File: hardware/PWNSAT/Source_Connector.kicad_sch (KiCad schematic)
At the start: 4 parts

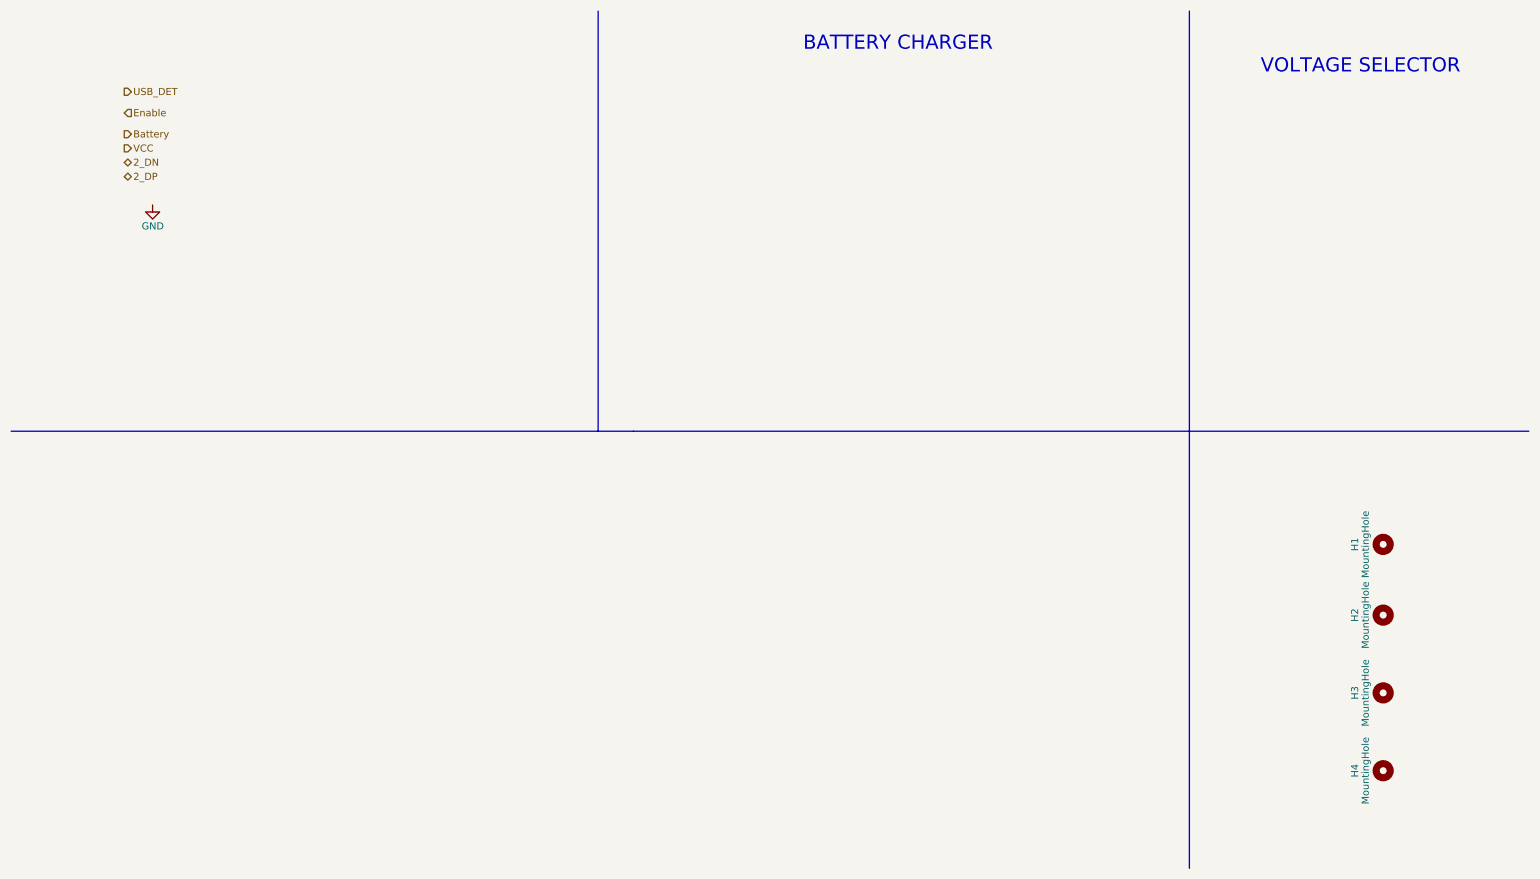
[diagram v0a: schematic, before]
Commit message: feat(Hw):Update_Battery_Sch_And_Sensors_And_PWNCube
pending_Outputs_connectors
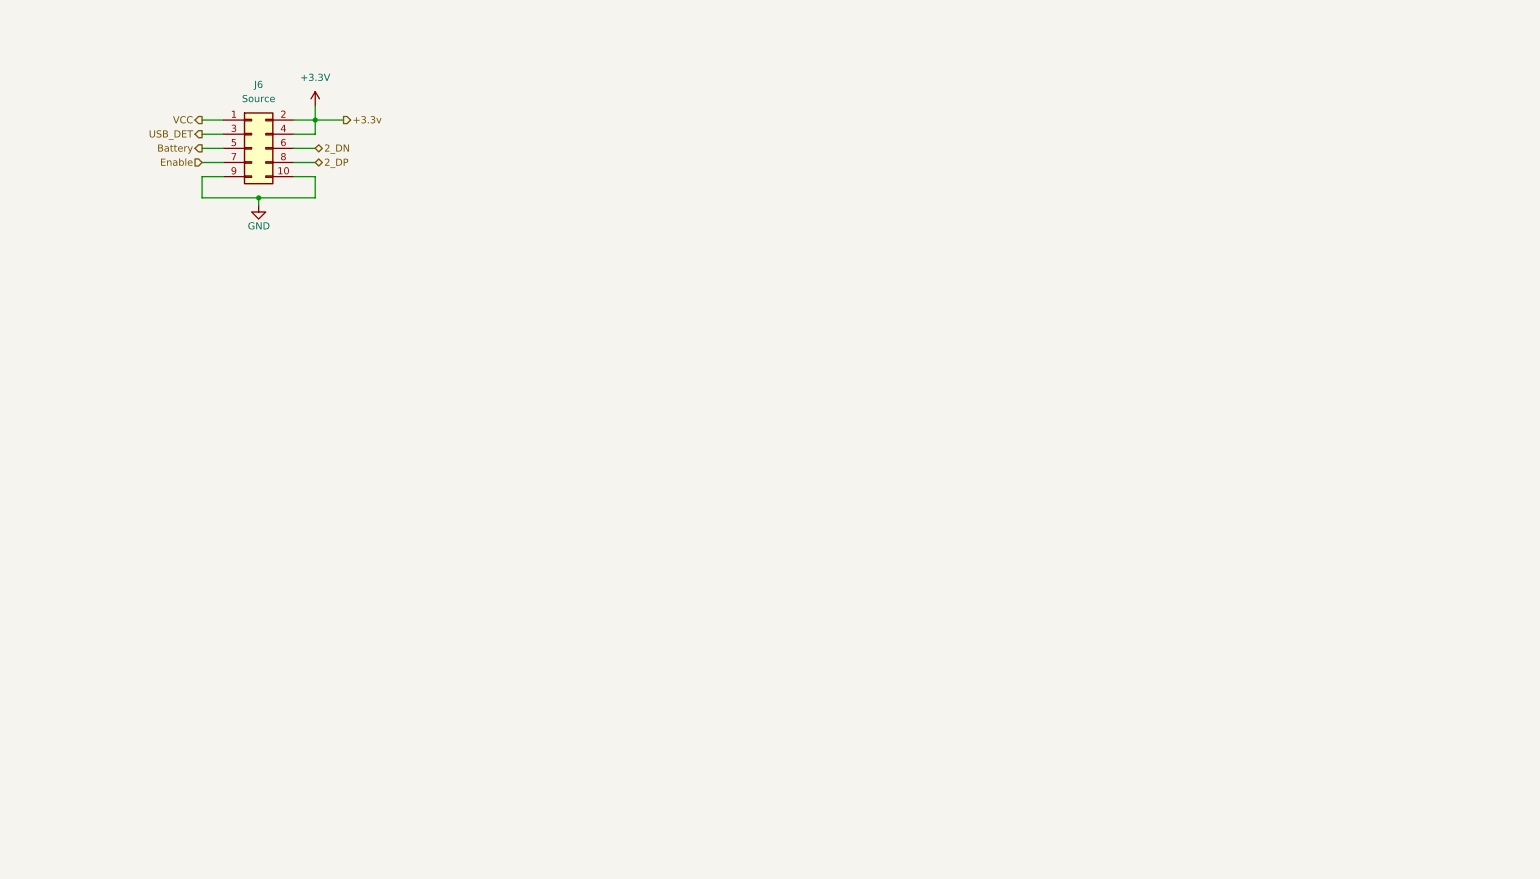
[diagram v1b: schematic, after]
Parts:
- removed H1, H2, H3, H4: MountingHole, MountingHole:MountingHole_2.2mm_M2, symbol Mechanical:MountingHole
- added J6: Source, symbol Connector_Generic:Conn_02x05_Odd_Even
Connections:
- net 2_DN: now also J6.6 (Pin_6)
- net 2_DP: now also J6.8 (Pin_8)
- net Battery: now also J6.5 (Pin_5)
- net Enable: now also J6.7 (Pin_7)
- net GND: now also J6.10 (Pin_10), J6.9 (Pin_9)
- net USB_DET: now also J6.3 (Pin_3)
- net VCC: now also J6.1 (Pin_1)
- new net +3.3V: J6.2 (Pin_2), J6.4 (Pin_4)
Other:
- note removed: "BATTERY CHARGER"
- note removed: "VOLTAGE SELECTOR"
- company: (none) -> Electronic Cats
- title: (none) -> PWNCube

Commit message: feat(Hw):BoM´s_Updated
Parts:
- J6: footprint (none) -> Connector_PinHeader_2.54mm:PinHeader_2x05_P2.54mm_Vertical; LCSC# (none) -> C7501191
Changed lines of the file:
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@@
 			)
 		)
-		(property "Footprint" ""
+		(property "Footprint" "Connector_PinHeader_2.54mm:PinHeader_2x05_P2.54mm_Vertical"
 			(at 54.61 36.83 0)
 			(effects
@@
 			(at 54.61 36.83 0)
 			(effects
+				(font
+					(size 1.27 1.27)
+				)
+				(hide yes)
+			)
+		)
+		(property "Proveedor" ""
+			(at 54.61 36.83 0)
+			(effects
+				(font
+					(size 1.27 1.27)
+				)
+				(hide yes)
+			)
+		)
+		(property "LCSC#" "C7501191"
+			(at 54.61 36.83 0)
+			(effects

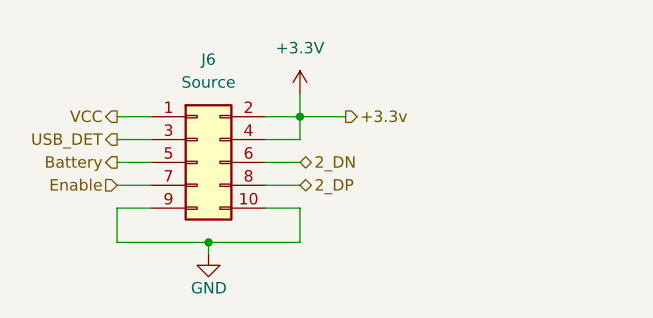
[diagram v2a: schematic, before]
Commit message: Feat(Hw): Change to 4-layer
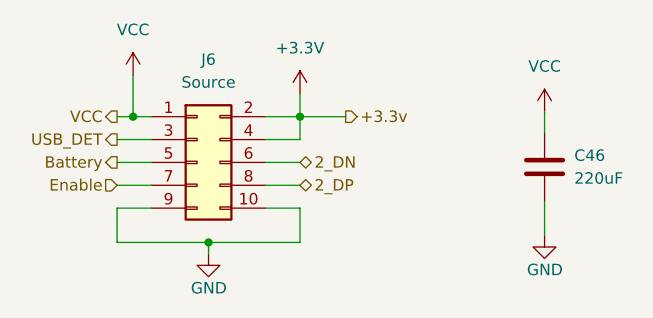
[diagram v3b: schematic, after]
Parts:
- added C46: 220uF, Capacitor_SMD:C_1206_3216Metric, symbol Device:C
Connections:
- net GND: now also C46.2
- net VCC: now also C46.1
